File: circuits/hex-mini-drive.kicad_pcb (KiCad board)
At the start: 2 copper layers, 19 parts

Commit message: Tentatively complete the PCB layout.
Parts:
- added C10: 100nF, components_footprints:C0603, F.Cu at (51.8, 64.8)
- added C11: 100nF, components_footprints:C0603, F.Cu at (55.0, 64.8)
- added C12: 100nF, components_footprints:C0603, F.Cu at (59.8, 75.5)
- added C13: 100nF, components_footprints:C0603, F.Cu at (60.5, 65.5)
- added C14: 10uF, components_footprints:C1206, F.Cu at (52.8, 102.6)
- added C15: 10uF, components_footprints:C1206, F.Cu at (52.8, 106.2)
- added C16: 10uF, components_footprints:C1206, F.Cu at (52.8, 108.5)
- added C17: 10uF, components_footprints:C1206, F.Cu at (52.8, 110.8)
- added C18: 30pF, components_footprints:C0603, F.Cu at (59.8, 78.5)
- added C19: 30pF, components_footprints:C0603, F.Cu at (51.2, 78.5)
- added C2: 10nF, components_footprints:C0805, F.Cu at (56.8, 87.4)
- added C20: 100nF, components_footprints:C0603, F.Cu at (51.2, 75.5)
- added C21: 100nF, components_footprints:C0603, F.Cu at (51.2, 81.5)
- added C22: 100nF, components_footprints:C0603, F.Cu at (55.7, 90.5)
- added C23: 10uF, components_footprints:C1206, F.Cu at (52.8, 113.1)
- added C3: 10nF, components_footprints:C0805, F.Cu at (58.8, 87.4)
- added C4: 0.1uF, components_footprints:C0805, F.Cu at (58.8, 82.8)
- added C5: 10uF, components_footprints:C1206, F.Cu at (52.8, 100.4)
- added C6: 1uF, components_footprints:C0603, F.Cu at (60.2, 58.2)
- added C7: 1uF, components_footprints:C0603, F.Cu at (58.1, 64.8)
- added C8: 100nF, components_footprints:C0603, F.Cu at (60.2, 60.0)
- added C9: 1uF, components_footprints:C0603, F.Cu at (60.2, 61.8)
- added CN2: ~, components_footprints:FPC-SMD_P0.50-16P_FGS-XJ-H2.0, F.Cu at (63.1, 74.5)
- added D2: ~, components_footprints:IN4148WS T4 SOD-323_L1.8-W1.3-LS2.5-RD, F.Cu at (53.0, 87.8)
- added D3: ~, components_footprints:IN4148WS T4 SOD-323_L1.8-W1.3-LS2.5-RD, F.Cu at (51.2, 87.8)
- added L1: 300mΩ, components_footprints:L0805, F.Cu at (51.2, 54.5)
- added L2: 10uH, components_footprints:L0805, F.Cu at (66.8, 54.5)
- added LED1: ~, components_footprints:LED-ARRAY-SMD_4P-L1.6-W1.5-BR_XL-1615RGBC-RF, F.Cu at (66.9, 66.6)
- added R10: 10Ω, components_footprints:R0603, F.Cu at (62.5, 89.8)
- added R11: 1.5kΩ, components_footprints:R0603, F.Cu at (60.3, 63.2)
- added R12: 1.5kΩ, components_footprints:R0603, F.Cu at (62.0, 66.5)
- added R13: 1.5kΩ, components_footprints:R0603, F.Cu at (63.5, 66.5)
- added R14: 1.5kΩ, components_footprints:R0603, F.Cu at (65.0, 66.5)
- added R20: 10kΩ, components_footprints:R0603, F.Cu at (54.2, 84.5)
- added R21: 47kΩ, components_footprints:R0603, F.Cu at (54.2, 81.5)
- added R22: 47kΩ, components_footprints:R0603, F.Cu at (52.8, 81.5)
- added R5: 10Ω, components_footprints:R0603, F.Cu at (67.0, 89.8)
- added R6: 10Ω, components_footprints:R0603, F.Cu at (65.5, 89.8)
- added R7: 10Ω, components_footprints:R0603, F.Cu at (64.0, 89.8)
- added R8: 10Ω, components_footprints:R0603, F.Cu at (58.7, 90.5)
- added R9: 10Ω, components_footprints:R0603, F.Cu at (61.0, 89.8)
- added U4: ~, components_footprints:AMS1117-3.3 SOT-223-3_L6.5-W3.4-P2.30-LS7.0-BR, F.Cu at (54.5, 60.5)
- C1: value ~ -> 10nF
- CN1: footprint components_footprints:FPC-SMD_KH-FG1.0-H2.0-8PIN -> components_footprints:FPC-SMD_P0.50-16P_FGS-XJ-H2.0
- R1, R2, R3: value ~ -> 500mW 10mΩ; footprint components_footprints:R1206 -> components_footprints:R0805
- R4: value ~ -> 100kΩ; footprint components_footprints:R1206 -> components_footprints:R0603
- moved R3 29.6 mm to (56.4, 112.0), turned to -90 degrees
- moved R2 28.1 mm to (56.4, 107.2), turned to -90 degrees
- moved R1 26.6 mm to (56.4, 102.4), turned to -90 degrees
- moved Q5 19.0 mm to (65.2, 111.0)
- moved X1 13.9 mm to (55.5, 78.0), turned to 180 degrees
- moved U2 13.8 mm to (53.8, 95.3), turned to 180 degrees
- moved D1 13.3 mm to (54.6, 87.8), turned to -90 degrees
- moved Q3 12.8 mm to (65.2, 103.2)
- moved Q1 12.7 mm to (65.2, 95.3)
- moved Q6 11.3 mm to (59.9, 111.0)
- moved U3 10.8 mm to (63.8, 84.8), turned to -90 degrees
- moved CN3 9.75 mm to (58.9, 117.4)
- moved Q2 8.95 mm to (59.9, 95.3)
- moved C1 5.96 mm to (56.8, 82.8), turned to 90 degrees
- moved U1 2.80 mm to (55.5, 70.8), turned to -90 degrees
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- renumbered P1 to CN3, U2 to CN4, U4 to U1, U3 to U2, U1 to U3
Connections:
- C1 pad 1: unconnected-(C1-Pad1) -> OUT1
- C1 pad 2: unconnected-(C1-Pad2) -> /Boost Gate 1
- CN1 pad 1: unconnected-(CN1-Pad1) -> +5V
- CN1 pad 10: unconnected-(CN1-Pad10) -> GND
- CN1 pad 2: unconnected-(CN1-Pad2) -> USART1_TX
- CN1 pad 3: unconnected-(CN1-Pad3) -> USART1_RX
- CN1 pad 4: unconnected-(CN1-Pad4) -> GPIO_Input_CS
- CN1 pad 5: unconnected-(CN1-Pad5) -> BOOT0
- CN1 pad 6: unconnected-(CN1-Pad6) -> NRST
- CN1 pad 7: unconnected-(CN1-Pad7) -> GND
- CN1 pad 8: unconnected-(CN1-Pad8) -> GND
- CN1 pad 9: unconnected-(CN1-Pad9) -> GND
- CN3 pad 1: unconnected-(P1-Pad1) -> TIM2_CH1/H1
- CN3 pad 2: unconnected-(P1-Pad2) -> TIM2_CH2/H2
- CN3 pad 3: unconnected-(P1-Pad3) -> TIM2_CH3/H3
- CN3 pad 4: unconnected-(P1-Pad4) -> GND
- CN3 pad 5: unconnected-(P1-Pad5) -> +3V3
- CN3 pad 6: unconnected-(P1-Pad6) -> OUT1
- CN3 pad 7: unconnected-(P1-Pad7) -> OUT2
- CN3 pad 8: unconnected-(P1-Pad8) -> OUT3
- CN4 pad 1: unconnected-(U2-VCC-Pad1) -> +5V
- CN4 pad 2: unconnected-(U2-D--Pad2) -> USB_D-
- CN4 pad 3: unconnected-(U2-D+-Pad3) -> USB_D+
- CN4 pad 5: unconnected-(U2-GND-Pad5) -> GND
- D1 pad 1: unconnected-(D1-K-Pad1) -> /Boost Gate 1
- D1 pad 2: unconnected-(D1-A-Pad2) -> +VDC
- Q1 pad 1: unconnected-(Q1-S-Pad1) -> SHUNT1
- Q1 pad 2: unconnected-(Q1-S-Pad2) -> SHUNT1
- Q1 pad 3: unconnected-(Q1-S-Pad3) -> SHUNT1
- Q1 pad 4: unconnected-(Q1-G-Pad4) -> GATE1H
- Q1 pad 5: unconnected-(Q1-D-Pad5) -> +VDC
- Q1 pad 6: unconnected-(Q1-D-Pad6) -> +VDC
- Q1 pad 7: unconnected-(Q1-D-Pad7) -> +VDC
- Q1 pad 8: unconnected-(Q1-D-Pad8) -> +VDC
- Q2 pad 1: unconnected-(Q2-S-Pad1) -> GND
- Q2 pad 2: unconnected-(Q2-S-Pad2) -> GND
- Q2 pad 3: unconnected-(Q2-S-Pad3) -> GND
- Q2 pad 4: unconnected-(Q2-G-Pad4) -> GATE1L
- Q2 pad 5: unconnected-(Q2-D-Pad5) -> SHUNT1
- Q2 pad 6: unconnected-(Q2-D-Pad6) -> SHUNT1
- Q2 pad 7: unconnected-(Q2-D-Pad7) -> SHUNT1
- Q2 pad 8: unconnected-(Q2-D-Pad8) -> SHUNT1
- Q3 pad 1: unconnected-(Q3-S-Pad1) -> SHUNT2
- Q3 pad 2: unconnected-(Q3-S-Pad2) -> SHUNT2
- Q3 pad 3: unconnected-(Q3-S-Pad3) -> SHUNT2
- Q3 pad 4: unconnected-(Q3-G-Pad4) -> GATE2H
- Q3 pad 5: unconnected-(Q3-D-Pad5) -> +VDC
- Q3 pad 6: unconnected-(Q3-D-Pad6) -> +VDC
- Q3 pad 7: unconnected-(Q3-D-Pad7) -> +VDC
- Q3 pad 8: unconnected-(Q3-D-Pad8) -> +VDC
- Q4 pad 1: unconnected-(Q4-S-Pad1) -> GND
- Q4 pad 2: unconnected-(Q4-S-Pad2) -> GND
- Q4 pad 3: unconnected-(Q4-S-Pad3) -> GND
- Q4 pad 4: unconnected-(Q4-G-Pad4) -> GATE2L
- Q4 pad 5: unconnected-(Q4-D-Pad5) -> SHUNT2
- Q4 pad 6: unconnected-(Q4-D-Pad6) -> SHUNT2
- Q4 pad 7: unconnected-(Q4-D-Pad7) -> SHUNT2
- Q4 pad 8: unconnected-(Q4-D-Pad8) -> SHUNT2
- Q5 pad 1: unconnected-(Q5-S-Pad1) -> SHUNT3
- Q5 pad 2: unconnected-(Q5-S-Pad2) -> SHUNT3
- Q5 pad 3: unconnected-(Q5-S-Pad3) -> SHUNT3
- Q5 pad 4: unconnected-(Q5-G-Pad4) -> GATE3H
- Q5 pad 5: unconnected-(Q5-D-Pad5) -> +VDC
- Q5 pad 6: unconnected-(Q5-D-Pad6) -> +VDC
- Q5 pad 7: unconnected-(Q5-D-Pad7) -> +VDC
- Q5 pad 8: unconnected-(Q5-D-Pad8) -> +VDC
- Q6 pad 1: unconnected-(Q6-S-Pad1) -> GND
- Q6 pad 2: unconnected-(Q6-S-Pad2) -> GND
- Q6 pad 3: unconnected-(Q6-S-Pad3) -> GND
- Q6 pad 4: unconnected-(Q6-G-Pad4) -> GATE3L
- Q6 pad 5: unconnected-(Q6-D-Pad5) -> SHUNT3
- Q6 pad 6: unconnected-(Q6-D-Pad6) -> SHUNT3
- Q6 pad 7: unconnected-(Q6-D-Pad7) -> SHUNT3
- Q6 pad 8: unconnected-(Q6-D-Pad8) -> SHUNT3
- R1 pad 1: unconnected-(R1-Pad1) -> SHUNT1
- R1 pad 2: unconnected-(R1-Pad2) -> OUT1
- R2 pad 1: unconnected-(R2-Pad1) -> SHUNT2
- R2 pad 2: unconnected-(R2-Pad2) -> OUT2
- R3 pad 1: unconnected-(R3-Pad1) -> SHUNT3
- R3 pad 2: unconnected-(R3-Pad2) -> OUT3
- R4 pad 1: unconnected-(R4-Pad1) -> ADC1_IN6
- R4 pad 2: unconnected-(R4-Pad2) -> +VDC
- U1 pad 1: unconnected-(U4-VBAT-Pad1) -> +3V3
- U1 pad 10: unconnected-(U4-PA0-WKUP-Pad10) -> TIM2_CH1/H1
- U1 pad 11: unconnected-(U4-PA1-Pad11) -> TIM2_CH2/H2
- U1 pad 12: unconnected-(U4-PA2-Pad12) -> ADC1_IN2
- U1 pad 13: unconnected-(U4-PA3-Pad13) -> ADC1_IN3
- U1 pad 14: unconnected-(U4-PA4-Pad14) -> ADC1_IN4
- U1 pad 15: unconnected-(U4-PA5-Pad15) -> ADC1_IN5/REF
- U1 pad 16: unconnected-(U4-PA6-Pad16) -> ADC1_IN6
- U1 pad 17: unconnected-(U4-PA7-Pad17) -> TIM1_CH1N
- U1 pad 18: unconnected-(U4-PB0-Pad18) -> TIM1_CH2N
- U1 pad 19: unconnected-(U4-PB1-Pad19) -> TIM1_CH3N
- U1 pad 2: unconnected-(U4-PC13-TAMPER-RTC-Pad2) -> GPIO_Input_A
- U1 pad 20: unconnected-(U4-PB2-Pad20) -> GPIO_Input_CS
- U1 pad 21: unconnected-(U4-PB10-Pad21) -> TIM2_CH3/H3
- U1 pad 22: unconnected-(U4-PB11-Pad22) -> TIM2_CH4
- U1 pad 23: unconnected-(U4-VSS_1-Pad23) -> GND
- U1 pad 24: unconnected-(U4-VDD_1-Pad24) -> +3V3
- U1 pad 25: unconnected-(U4-PB12-Pad25) -> SPI2_NSS
- U1 pad 26: unconnected-(U4-PB13-Pad26) -> SPI2_SCK
- U1 pad 27: unconnected-(U4-PB14-Pad27) -> SPI2MISO
- U1 pad 28: unconnected-(U4-PB15-Pad28) -> SPI2_MOSI
- U1 pad 29: unconnected-(U4-PA8-Pad29) -> TIM1_CH1
- U1 pad 3: unconnected-(U4-PC14-OSC32_IN-Pad3) -> GPIO_Input_B
- U1 pad 30: unconnected-(U4-PA9-Pad30) -> TIM1_CH2
- U1 pad 31: unconnected-(U4-PA10-Pad31) -> TIM1_CH3
- U1 pad 32: unconnected-(U4-PA11-Pad32) -> USB_D-
- U1 pad 33: unconnected-(U4-PA12-Pad33) -> USB_D+
- U1 pad 34: unconnected-(U4-PA13-Pad34) -> SYS_JTMS-SWDIO
- U1 pad 35: unconnected-(U4-VSS_2-Pad35) -> GND
- U1 pad 36: unconnected-(U4-VDD_2-Pad36) -> +3V3
- U1 pad 37: unconnected-(U4-PA14-Pad37) -> SYS_JTCK-SWCLK
- U1 pad 38: unconnected-(U4-PA15-Pad38) -> SYS_JTDI
- U1 pad 39: unconnected-(U4-PB3-Pad39) -> SYS_JTDO-TRACESWO
- U1 pad 4: unconnected-(U4-PC15-OSC32_OUT-Pad4) -> GPIO_Input_C
- U1 pad 40: unconnected-(U4-PB4-Pad40) -> TIM3_CH1
- U1 pad 41: unconnected-(U4-PB5-Pad41) -> TIM3_CH2
- U1 pad 42: unconnected-(U4-PB6-Pad42) -> USART1_TX
- U1 pad 43: unconnected-(U4-PB7-Pad43) -> USART1_RX
- U1 pad 44: unconnected-(U4-BOOT0-Pad44) -> BOOT0
- U1 pad 45: unconnected-(U4-PB8-Pad45) -> I2C1_SCL
- U1 pad 46: unconnected-(U4-PB9-Pad46) -> I2C1_SDA
- U1 pad 47: unconnected-(U4-VSS_3-Pad47) -> GND
- U1 pad 48: unconnected-(U4-VDD_3-Pad48) -> +3V3
- U1 pad 5: unconnected-(U4-PD0-OSC_IN-Pad5) -> /RCC_OSC_IN
- U1 pad 6: unconnected-(U4-PD1-OSC_OUT-Pad6) -> /RCC_OSC_OUT
- U1 pad 7: unconnected-(U4-NRST-Pad7) -> NRST
- U1 pad 8: unconnected-(U4-VSSA-Pad8) -> GND
- U1 pad 9: unconnected-(U4-VDDA-Pad9) -> +3V3A
- U2 pad 1: unconnected-(U3-REF1-Pad1) -> ADC1_IN5/REF
- U2 pad 12: unconnected-(U3-REF3-Pad12) -> ADC1_IN5/REF
- U2 pad 13: unconnected-(U3-OUT3-Pad13) -> ADC1_IN4
- U2 pad 14: unconnected-(U3-IN±3-Pad14) -> SHUNT3
- U2 pad 15: unconnected-(U3-IN+3-Pad15) -> OUT3
- U2 pad 16: unconnected-(U3-GND-Pad16) -> GND
- U2 pad 2: unconnected-(U3-OUT1-Pad2) -> ADC1_IN2
- U2 pad 20: unconnected-(U3-REF4-Pad20) -> ADC1_IN5/REF
- U2 pad 3: unconnected-(U3-IN±1-Pad3) -> SHUNT1
- U2 pad 4: unconnected-(U3-IN+1-Pad4) -> OUT1
- U2 pad 5: unconnected-(U3-VS-Pad5) -> +3V3
- U2 pad 6: unconnected-(U3-IN+2-Pad6) -> SHUNT2
- U2 pad 7: unconnected-(U3-IN±2-Pad7) -> OUT2
- U2 pad 8: unconnected-(U3-OUT2-Pad8) -> ADC1_IN3
- U2 pad 9: unconnected-(U3-REF2-Pad9) -> ADC1_IN5/REF
- U3 pad 1: unconnected-(U1-HIN1-Pad1) -> TIM1_CH1
- U3 pad 10: unconnected-(U1-LO2-Pad10) -> /LO2
- U3 pad 11: unconnected-(U1-LO1-Pad11) -> /LO1
- U3 pad 12: unconnected-(U1-VS3-Pad12) -> OUT3
- U3 pad 13: unconnected-(U1-HO3-Pad13) -> /HO3
- U3 pad 14: unconnected-(U1-VB3-Pad14) -> /Boost Gate 3
- U3 pad 15: unconnected-(U1-VS2-Pad15) -> OUT2
- U3 pad 16: unconnected-(U1-HO2-Pad16) -> /HO2
- U3 pad 17: unconnected-(U1-VB2-Pad17) -> /Boost Gate 2
- U3 pad 18: unconnected-(U1-VS1-Pad18) -> OUT1
- U3 pad 19: unconnected-(U1-HO1-Pad19) -> /HO1
- U3 pad 2: unconnected-(U1-HIN2-Pad2) -> TIM1_CH2
- U3 pad 20: unconnected-(U1-VB1-Pad20) -> /Boost Gate 1
- U3 pad 3: unconnected-(U1-HIN3-Pad3) -> TIM1_CH3
- U3 pad 4: unconnected-(U1-LIN1-Pad4) -> TIM1_CH1N
- U3 pad 5: unconnected-(U1-LIN2-Pad5) -> TIM1_CH2N
- U3 pad 6: unconnected-(U1-LIN3-Pad6) -> TIM1_CH3N
- U3 pad 7: unconnected-(U1-VCC-Pad7) -> +VDC
- U3 pad 8: unconnected-(U1-COM-Pad8) -> GND
- U3 pad 9: unconnected-(U1-LO3-Pad9) -> /LO3
- X1 pad 1: unconnected-(X1-OSC1-Pad1) -> /RCC_OSC_IN
- X1 pad 2: unconnected-(X1-OSC2-Pad2) -> /RCC_OSC_OUT
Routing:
- net +3V3: track 0.00 -> 139.8 mm, vias 0 -> 12
- net GND: track 0.00 -> 81.5 mm, vias 0 -> 43
- net OUT3: track 0.00 -> 80.3 mm, vias 0 -> 5
- net OUT2: track 0.00 -> 60.5 mm, vias 0 -> 4
- net TIM2_CH3/H3: track 0.00 -> 58.9 mm, vias 0 -> 1
- net +3V3A: track 0.00 -> 58.8 mm, vias 0 -> 3
- net +VDC: track 0.00 -> 57.1 mm, vias 0 -> 27
- net OUT1: track 0.00 -> 56.7 mm, vias 0 -> 4
- net TIM2_CH1/H1: track 0.00 -> 55.8 mm, vias 0 -> 1
- net TIM2_CH2/H2: track 0.00 -> 50.2 mm, vias 0 -> 1
- net ADC1_IN5/REF: track 0.00 -> 41.5 mm, vias 0 -> 4
- net +5V: track 0.00 -> 38.1 mm, vias 0 -> 3
- net SHUNT3: track 0.00 -> 35.2 mm, vias 0 -> 2
- net NRST: track 0.00 -> 34.6 mm, vias 0 -> 2
- net SHUNT2: track 0.00 -> 32.1 mm, vias 0 -> 2
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- added copper zone on In2.Cu, net +VDC
- added copper zone on In1.Cu, net GND
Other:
- board outline added: 18 x 80 mm
- copper layers 2 -> 4

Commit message: Finalise mini drive test circuit and generate production files.
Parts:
- moved C12 0.29 mm to (60.1, 75.4), turned to -90 degrees
- moved CN4 0.10 mm to (64.4, 60.8)
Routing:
- net SHUNT3: track 35.2 -> 38.6 mm
- net /Boost Gate 3: track 22.2 -> 18.9 mm
- net /Boost Gate 1: track 20.5 -> 22.7 mm
- net +5V: track 38.1 -> 40.2 mm
- net USB_D-: track 13.8 -> 15.5 mm
- net +VDC: track 57.1 -> 58.8 mm
- net OUT3: track 80.3 -> 81.9 mm
- net GATE2H: track 21.0 -> 19.5 mm
- net GND: track 81.5 -> 83.0 mm
- net +3V3: track 139.8 -> 140.9 mm

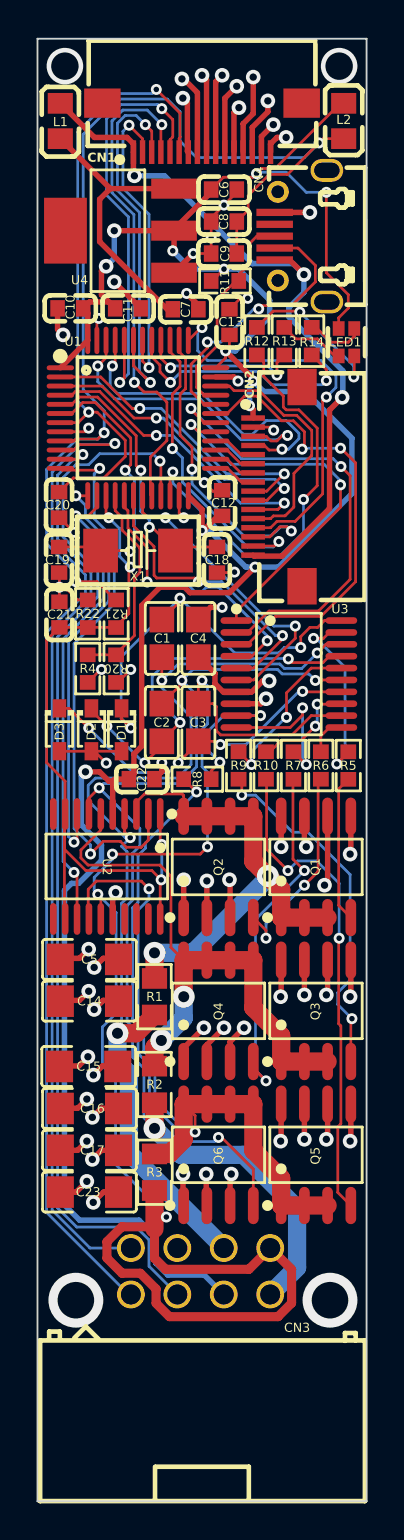
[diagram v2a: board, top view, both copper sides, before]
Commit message: Redo design with minimum 0.2mm line width and spacing.
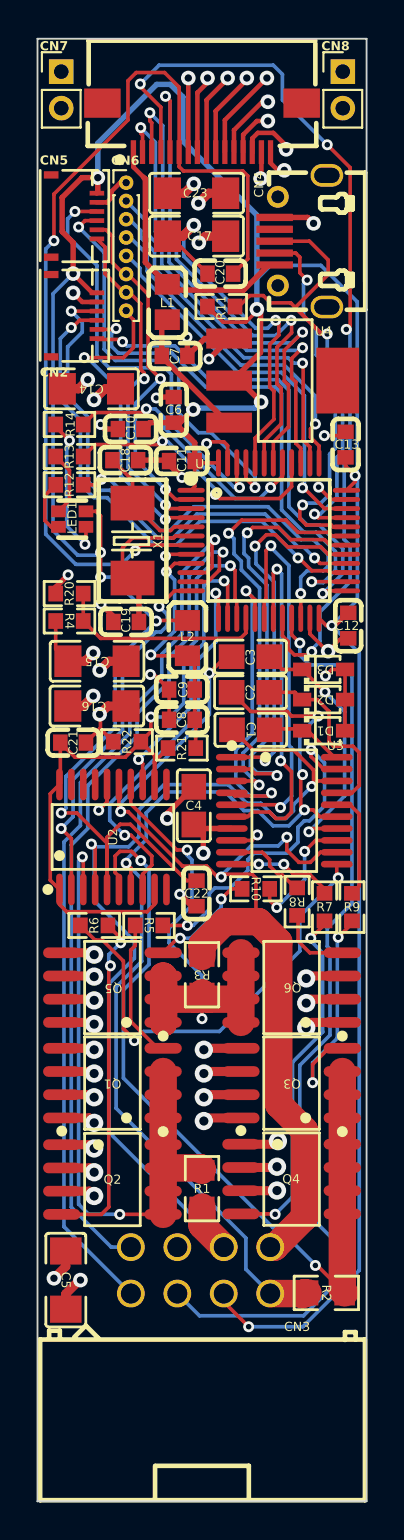
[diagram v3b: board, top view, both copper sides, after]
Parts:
- added CN5: ~, components_footprints:FPC-SMD_6P-P0.50_L3.8-W5.0, F.Cu at (52.0, 59.7)
- added CN6: Conn_01x08_Pin, components_footprints:PinHeader_1x08_P1.00mm_Vertical, F.Cu at (54.9, 57.9)
- added CN7: Conn_01x02_Pin, components_footprints:PinHeader_1x02_P2.00mm_Vertical, F.Cu at (51.3, 51.8)
- added CN8: Conn_01x02_Pin, components_footprints:PinHeader_1x02_P2.00mm_Vertical, F.Cu at (66.7, 51.8)
- CN2: footprint components_footprints:FPC-SMD_P0.50-16P_FGS-XJ-H2.0 -> components_footprints:FPC-SMD_6P-P0.50_L3.8-W5.0
- moved C23 54.9 mm to (58.7, 58.5)
- moved C17 50.3 mm to (58.7, 60.8)
- moved C14 33.5 mm to (53.0, 69.2), turned to 0 degrees
- moved L2 29.5 mm to (58.2, 82.8)
- moved C8 27.3 mm to (57.9, 87.2)
- moved C9 24.0 mm to (57.9, 85.6)
- moved C15 22.2 mm to (53.3, 84.0), turned to 0 degrees
- moved C16 22.0 mm to (53.2, 86.5), turned to 0 degrees
- moved Q2 18.1 mm to (54.1, 112.4), turned to -90 degrees
- moved LED1 17.8 mm to (51.9, 76.3), turned to 0 degrees
- moved C5 17.6 mm to (51.5, 117.9), turned to -90 degrees
- moved Q1 16.2 mm to (54.1, 107.1), turned to 90 degrees
- moved C20 15.4 mm to (60.0, 62.9), turned to 0 degrees
- moved R6 15.2 mm to (53.1, 98.5), turned to 0 degrees
- moved D3 14.8 mm to (65.7, 84.5), turned to 0 degrees
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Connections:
- CN2 pad 3: I2C1_SDA -> SPI2_MOSI
- CN2 pad 4: I2C1_SCL -> SPI2MISO
- CN2 pad 5: SPI2_MOSI -> SPI2_SCK
- CN2 pad 6: SPI2MISO -> SPI2_NSS
- CN2 pad 7: SPI2_SCK -> unconnected-(CN2-Pad7)
- CN2 pad 8: SPI2_NSS -> unconnected-(CN2-Pad8)
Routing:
- net +3V3: track 140.9 -> 186.1 mm
- net +3V3A: track 59.0 -> 14.1 mm, vias 3 -> 2
- net SPI2_MOSI: track 2.35 -> 28.8 mm, vias 0 -> 2
- net SPI2MISO: track 2.35 -> 28.5 mm, vias 0 -> 2
- net +5V: track 40.2 -> 14.6 mm, vias 3 -> 0
- net OUT3: track 81.9 -> 56.8 mm, vias 5 -> 4
- net SPI2_SCK: track 2.35 -> 27.3 mm, vias 0 -> 2
- net GATE3L: track 29.2 -> 4.24 mm, vias 2 -> 0
- net SPI2_NSS: track 2.35 -> 26.2 mm, vias 0 -> 2
- net GPIO_Input_CS: track 27.4 -> 50.6 mm, vias 2 -> 4
- net /LO1: track 2.17 -> 24.4 mm, vias 0 -> 2
- net GATE3H: track 27.1 -> 6.18 mm
- net NRST: track 34.6 -> 53.0 mm
- net /Boost Gate 1: track 22.7 -> 4.31 mm, vias 3 -> 0
- net USB_D+: track 12.0 -> 27.8 mm, vias 0 -> 2
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
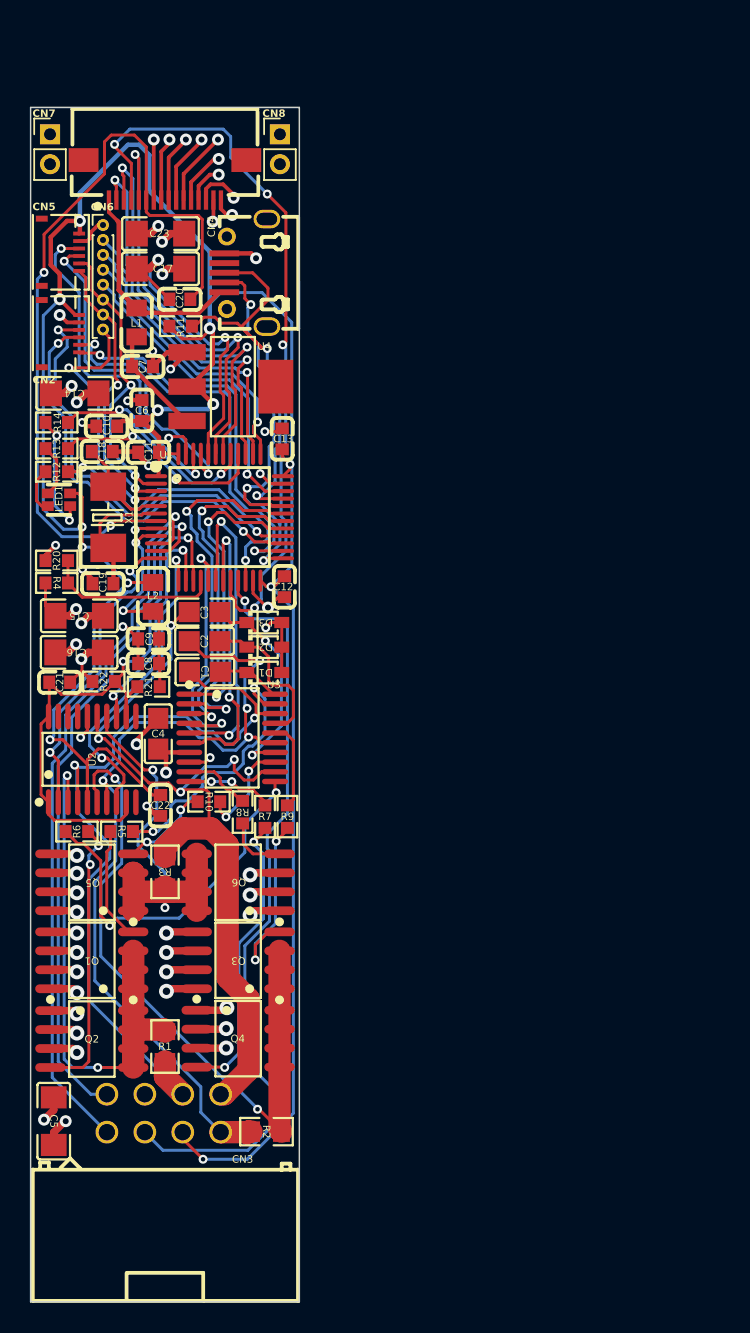
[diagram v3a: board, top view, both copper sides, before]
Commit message: Replan design with 2 sided IC components to make it more compact.
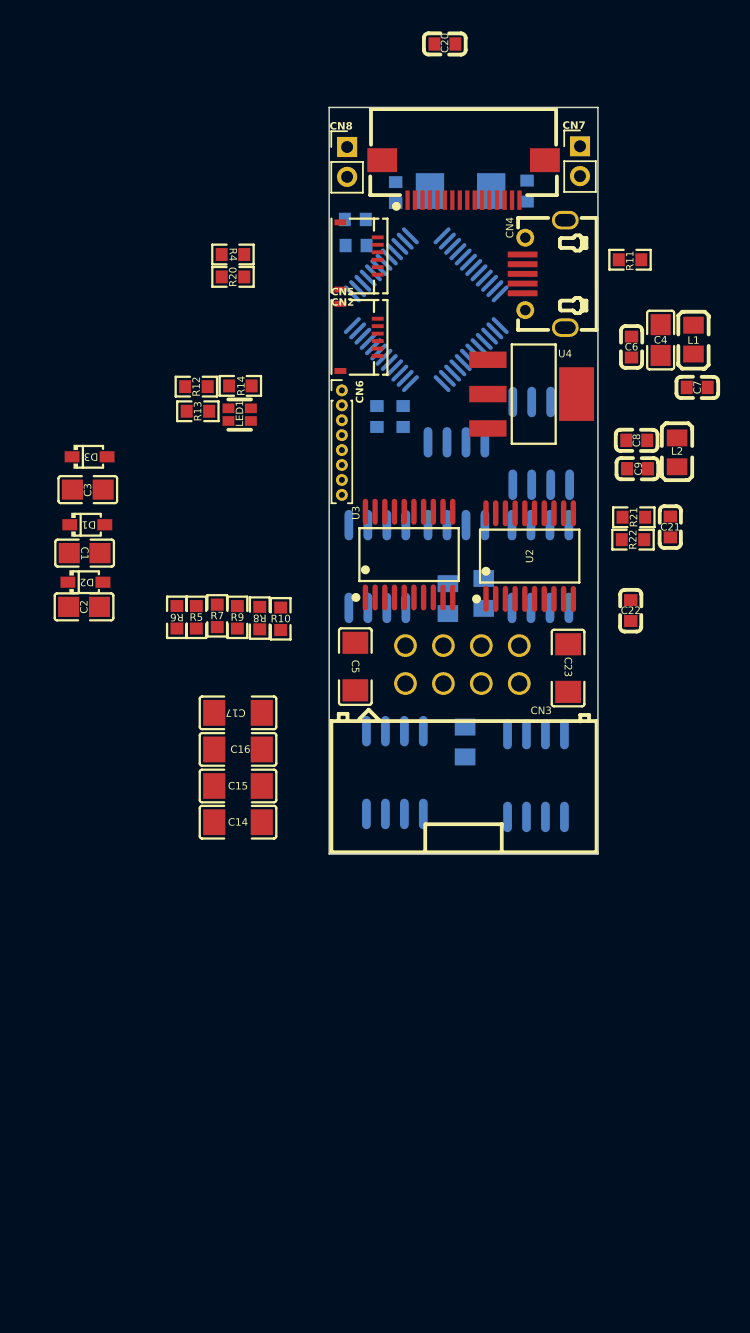
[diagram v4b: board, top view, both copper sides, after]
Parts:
- C10, C11, C12, C13, C18, C19, Q1, Q2, Q3, Q4, Q5, Q6, R1, R2, R3, U1, X1: moved to B.Cu
- moved C4 42.8 mm to (92.2, 65.6)
- moved C21 42.2 mm to (92.8, 78.1), turned to 90 degrees
- moved Q5 42.1 mm to (84.2, 72.5), turned to 180 degrees
- moved Q1 40.2 mm to (78.5, 75.2), turned to 180 degrees
- moved C23 39.9 mm to (86.0, 87.5), turned to 90 degrees
- moved C19 38.7 mm to (83.2, 55.6), turned to -90 degrees
- moved L1 37.3 mm to (94.4, 65.5)
- moved C7 37.2 mm to (94.7, 68.8)
- moved Q2 37.0 mm to (73.2, 80.8), turned to 180 degrees
- moved R22 36.7 mm to (90.3, 79.0)
- moved C5 36.5 mm to (71.8, 87.5)
- moved L2 36.4 mm to (93.3, 73.1)
- moved CN3 36.1 mm to (78.9, 87.3)
- moved C8 36.0 mm to (90.6, 72.3)
- moved CN7 35.5 mm to (86.8, 52.6)
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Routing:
- net +3V3: track 186.1 -> 0.00 mm, vias 12 -> 0
- net GND: track 95.6 -> 0.00 mm, vias 39 -> 0
- net OUT2: track 58.1 -> 0.00 mm, vias 4 -> 0
- net OUT3: track 56.8 -> 0.00 mm, vias 4 -> 0
- net +VDC: track 56.5 -> 0.00 mm, vias 25 -> 0
- net OUT1: track 55.1 -> 0.00 mm, vias 2 -> 0
- net NRST: track 53.0 -> 0.00 mm, vias 2 -> 0
- net TIM2_CH3/H3: track 50.8 -> 0.00 mm, vias 1 -> 0
- net GPIO_Input_CS: track 50.6 -> 0.00 mm, vias 4 -> 0
- net TIM2_CH1/H1: track 49.0 -> 0.00 mm, vias 1 -> 0
- net TIM2_CH2/H2: track 46.6 -> 0.00 mm, vias 1 -> 0
- net SHUNT2: track 45.4 -> 0.00 mm, vias 2 -> 0
- net ADC1_IN5/REF: track 41.6 -> 0.00 mm, vias 2 -> 0
- net SHUNT1: track 35.8 -> 0.00 mm, vias 2 -> 0
- net SPI2_MOSI: track 28.8 -> 0.00 mm, vias 2 -> 0
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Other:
- board size 18 x 80 mm -> 18 x 50 mm
